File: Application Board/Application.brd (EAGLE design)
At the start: 101.6 x 101.6 mm, 54 parts, among them Q1 DMP2012SN-7, T1 FDN340P, T2 AP1117_LIN_REG, U1 LM3409HV'LM3409HV', X1 22-23-2101

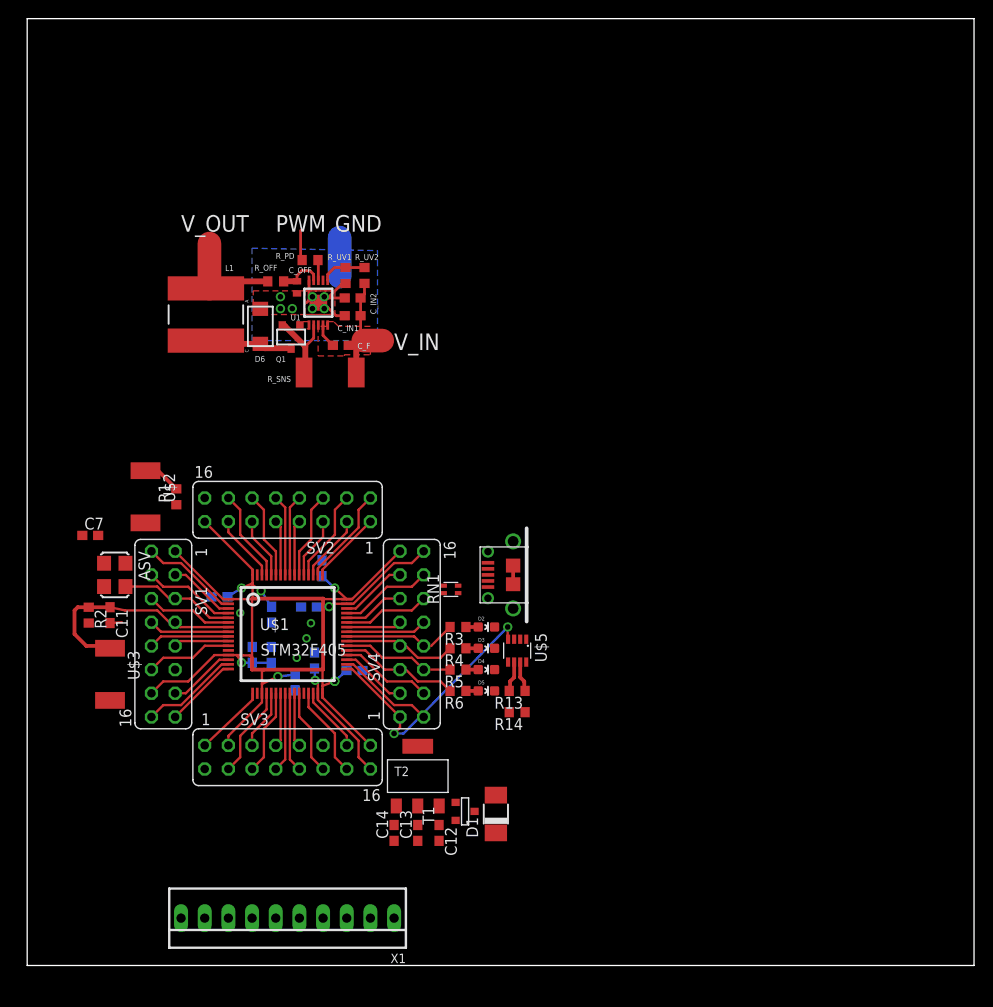
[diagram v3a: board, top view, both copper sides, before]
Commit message: Rearranged components, including LED driver.
Not finished, still need to fix LED driver and route the remaining
connector lines.
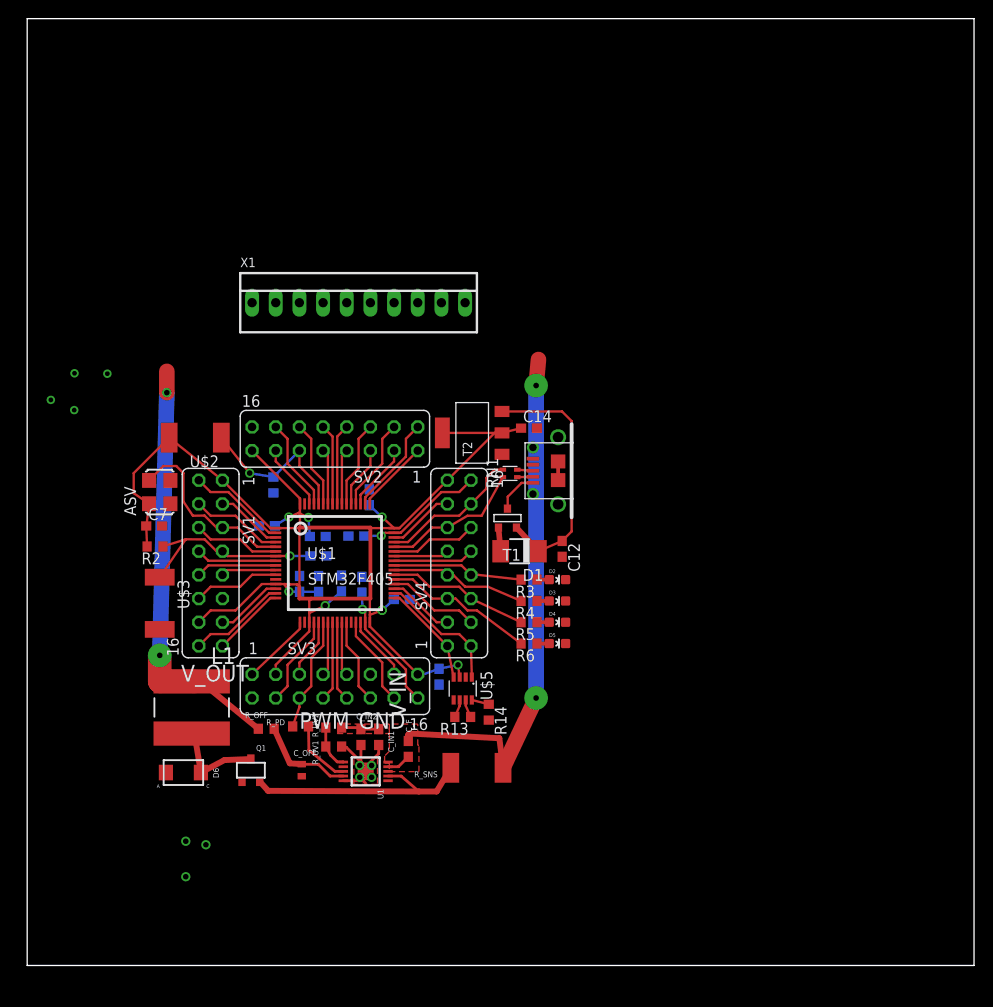
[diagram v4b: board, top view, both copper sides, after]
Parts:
- moved X1 66.5 mm to (35.6, 71.1), turned to 0 degrees
- moved C_OFF 51.8 mm to (29.5, 21.0)
- moved R_UV1 50.6 mm to (32.9, 23.5), turned to 180 degrees
- moved U1 50.5 mm to (36.3, 20.8), turned to 270 degrees
- moved R_PD 50.0 mm to (29.3, 25.7)
- moved R_UV2 48.6 mm to (32.9, 25.5), turned to 0 degrees
- moved D6 48.6 mm to (16.8, 20.7), turned to 180 degrees
- moved R_OFF 48.0 mm to (25.7, 25.4)
- moved C_IN2 47.1 mm to (35.8, 24.5), turned to 270 degrees
- moved Q1 46.7 mm to (24.0, 21.0), turned to 0 degrees
- moved C14 45.8 mm to (53.8, 57.7), turned to 0 degrees
- moved C_IN1 45.3 mm to (37.7, 24.5), turned to 270 degrees
- moved R_SNS 45.2 mm to (48.3, 21.2)
- moved C_F 43.9 mm to (40.9, 23.2), turned to 270 degrees
- moved L1 42.2 mm to (17.7, 27.7)
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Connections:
- removed net CAM_LED: SV3.6, U$1.22, X1.1
- removed net PWM: R_PD.1
- removed net V_IN: C_F.1, C_IN1.1, C_IN2.1, R_SNS.2, R_UV2.2, U1.10, U1.8
- removed net V_OUT: L1.2, R_OFF.1
- new net CAM_LEDV: L1.2, R_OFF.1, X1.1
- new net CAM_LED_PWM: R_PD.1, SV3.6, U$1.22
- net 12V: now also C_F.1, C_IN1.1, C_IN2.1, R_SNS.2, R_UV2.2, U1.10, U1.8
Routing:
- net 12V: track 0.00 -> 62.6 mm, vias 0 -> 2
- net CAM_LEDV: track 0.00 -> 51.5 mm, vias 0 -> 2
- net +3V3: track 115.3 -> 159.5 mm, vias 7 -> 8
- net N$58: track 0.00 -> 27.4 mm
- net N$8: track 8.91 -> 26.3 mm
- net CAN2_RX: track 28.2 -> 11.3 mm, vias 2 -> 0
- net V_OUT: track 16.8 -> 0.00 mm
- net CAM_LED_PWM: track 0.00 -> 12.4 mm
- net V_IN: track 12.3 -> 0.00 mm
- net CAM_LED: track 9.19 -> 0.00 mm
- net USBD-: track 6.57 -> 15.3 mm
- net OSCIN: track 12.4 -> 19.8 mm
- net BOOT0: track 11.0 -> 18.0 mm, vias 0 -> 1
- net GND: track 19.1 -> 13.3 mm
- net USBD+: track 9.95 -> 15.6 mm
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- added copper zone on layer 1, net 12V
- added copper zone on layer 1, net N$19
- removed copper zone on layer 16, net GND
- removed copper zone on layer 1, net N$10
- removed copper zone on layer 1, net V_IN

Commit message: updated stm... microcontroller to the updated version
organized order of output lines. Still not complete.
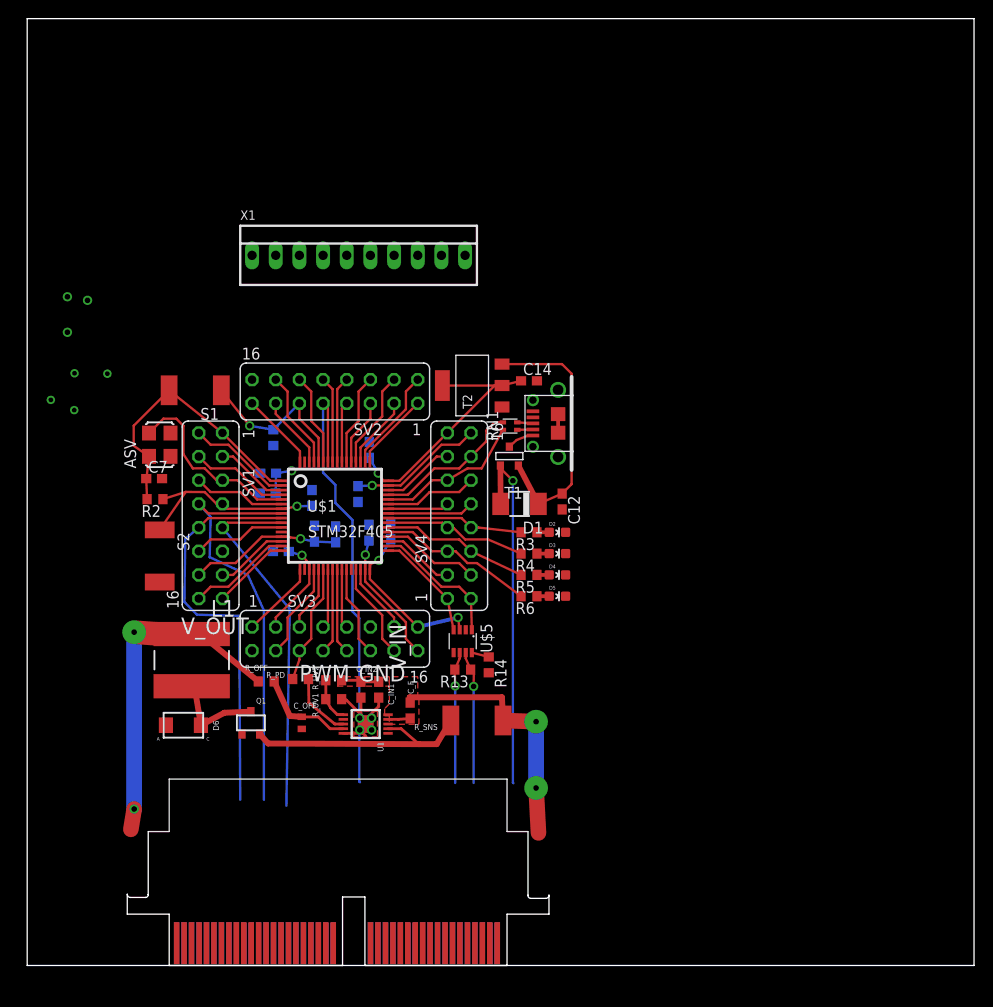
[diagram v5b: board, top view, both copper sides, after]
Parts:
- removed C13: 0.1uF, rcl:C0603
- removed U$2, U$3: SWITCH, DiscreteComponents:SW_2512
- added S1, S2: SWITCH, DiscreteComponents:SW_2512
- added U$6: HSCPART, Connectors:HSC8-40PINOUUT
- moved C4 7.40 mm to (39.0, 46.6), turned to 90 degrees
- moved C3 7.35 mm to (27.2, 44.4), turned to 0 degrees
- moved C8 7.11 mm to (25.8, 50.7), turned to 0 degrees
- moved T1 6.66 mm to (51.8, 54.7)
- moved C11 6.26 mm to (30.6, 50.2), turned to 90 degrees
- moved C6 5.64 mm to (25.9, 52.8)
- moved C1 5.64 mm to (36.7, 46.4)
- moved C10 5.62 mm to (30.8, 46.3)
- moved C9 5.61 mm to (33.1, 46.3)
- moved ASV 5.08 mm to (14.2, 55.9)
- moved C5 5.08 mm to (36.7, 55.3)
- moved D5 5.08 mm to (56.9, 39.6)
- moved R1 5.08 mm to (26.4, 56.6)
- moved R6 5.08 mm to (53.8, 39.6)
- moved RN1 5.08 mm to (51.8, 57.9)
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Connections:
- net +3V3: now also S1.2; no longer C13.1, U$2.2
- net BOOT0: now also S1.1; no longer U$2.1
- net GND: now also S2.2; no longer C13.2, U$3.2
- net NRST: now also S2.1; no longer U$3.1
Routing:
- net TEMP_SENS: track 5.93 -> 48.8 mm
- net +3V3: track 159.5 -> 118.0 mm, vias 8 -> 6
- net +5V: track 2.55 -> 38.7 mm, vias 0 -> 1
- net SHFT_REG_DATA: track 8.68 -> 44.5 mm
- net SHFT_REG_CLK: track 8.68 -> 44.1 mm
- net SHFT_REG_EN: track 5.93 -> 39.0 mm
- net 12V: track 62.6 -> 32.8 mm
- net CANH: track 1.93 -> 14.3 mm, vias 0 -> 1
- net CANL: track 1.93 -> 14.1 mm, vias 0 -> 1
- net CAM_LEDV: track 51.5 -> 42.2 mm
- net N$57: track 4.61 -> 2.89 mm
- net N$58: track 27.4 -> 28.6 mm
- net BOOT0: track 18.0 -> 18.6 mm
- net PIN59: track 9.32 -> 9.92 mm
- net PIN54: track 9.32 -> 9.92 mm
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
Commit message: Fixed output voltages and signal paths, added connector
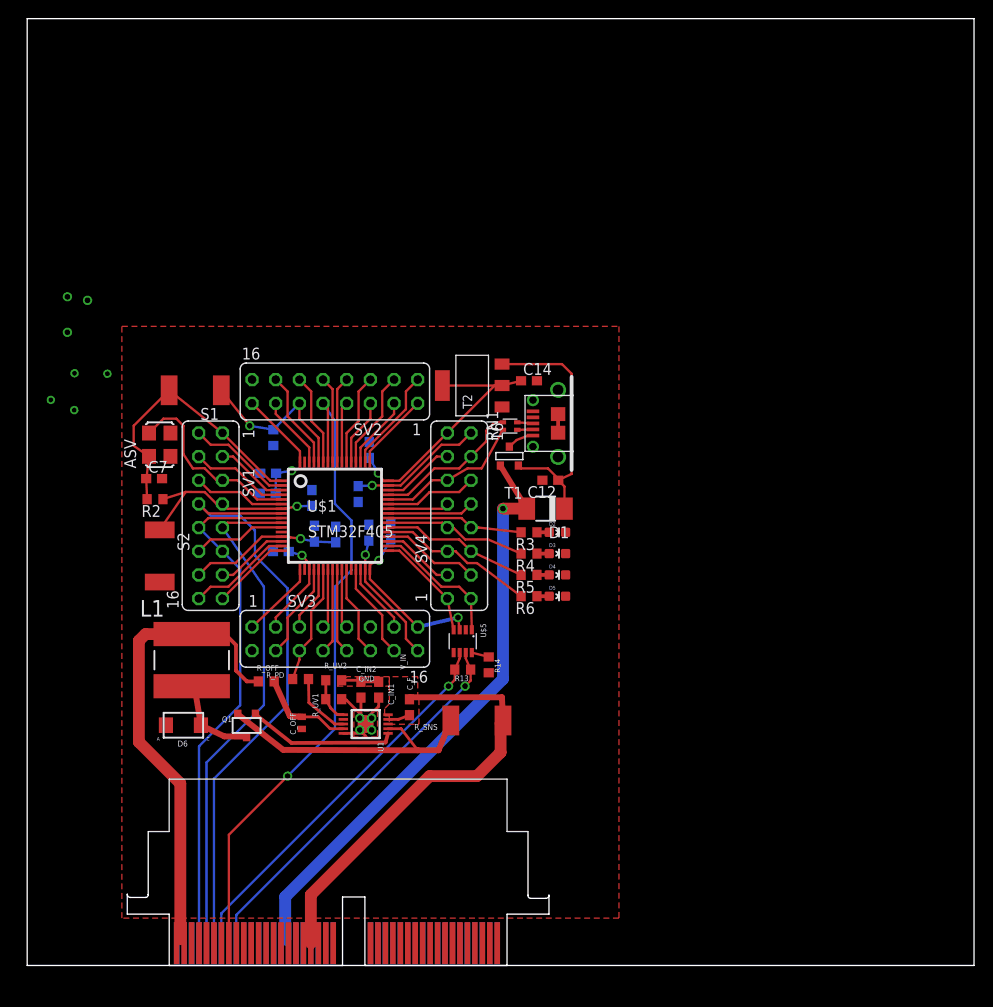
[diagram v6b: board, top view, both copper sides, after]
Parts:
- removed X1: 22-23-2101, con-molex:22-23-2101
- moved D1 2.84 mm to (55.6, 49.0)
- moved C12 2.62 mm to (56.1, 52.1), turned to 180 degrees
- moved Q1 0.54 mm to (23.5, 25.8), turned to 180 degrees
- moved C_F 0.36 mm to (41.0, 27.7)
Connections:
- net +5V: now also U$6.B15, U$6.B16; no longer X1.9
- net 12V: now also U$6.T18, U$6.T19, U$6.T20; no longer X1.10
- net CAM_LEDV: now also U$6.T1, U$6.T2; no longer X1.1
- net CANH: now also U$6.B9; no longer X1.7
- net CANL: now also U$6.B7; no longer X1.6
- net GND: now also U$6.T11, U$6.T12, U$6.T13; no longer X1.8
- net SHFT_REG_CLK: now also U$6.B4; no longer X1.3
- net SHFT_REG_DATA: now also U$6.B6; no longer X1.4
- net SHFT_REG_EN: now also U$6.B5; no longer X1.2
- net TEMP_SENS: now also U$6.T8; no longer X1.5
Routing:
- net CANL: track 14.1 -> 41.7 mm
- net CANH: track 14.3 -> 41.7 mm
- net +5V: track 38.7 -> 65.8 mm
- net TEMP_SENS: track 48.8 -> 71.0 mm, vias 0 -> 1
- net 12V: track 32.8 -> 54.0 mm, vias 2 -> 0
- net SHFT_REG_DATA: track 44.5 -> 65.5 mm
- net SHFT_REG_EN: track 39.0 -> 55.1 mm
- net N$10: track 0.00 -> 16.1 mm
- net SHFT_REG_CLK: track 44.1 -> 57.5 mm
- net CAM_LEDV: track 42.2 -> 52.1 mm, vias 2 -> 0
- net N$8: track 26.3 -> 30.7 mm
- net L1: track 10.1 -> 9.56 mm
- added copper zone on layer 1, net N$20
- removed copper zone on layer 1, net N$19
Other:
- board text removed: "PWM"
- board text removed: "V_OUT"

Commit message: Fixed up some wiring
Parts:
- renumbered U$6 to U$2
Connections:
- removed net 12V: C_F.1, C_IN1.1, C_IN2.1, R_SNS.2, R_UV2.2, U$2.T18, U$2.T19, U$2.T20, U1.10, U1.8
- new net +12V: C_F.1, C_IN1.1, C_IN2.1, R_SNS.2, R_UV2.2, U$2.T10, U$2.T11, U$2.T12, U$2.T13, U$2.T7, U$2.T8, U$2.T9, U1.10, U1.8
- net +3V3: now also U$2.B24
- net +5V: now also U$2.B1, U$2.B2, U$2.B3, U$2.B4, U$2.B5, U$2.B6; no longer U$2.B15, U$2.B16
- net CAM_LEDV: no longer U$2.T1, U$2.T2
- net CANH: now also U$2.B35; no longer U$2.B9
- net CANL: now also U$2.B33; no longer U$2.B7
- net GND: now also U$2.T14, U$2.T15, U$2.T16, U$2.T17, U$2.T18, U$2.T19, U$2.T20; no longer U$2.T11, U$2.T12, U$2.T13
- net SHFT_REG_CLK: no longer U$2.B4
- net SHFT_REG_DATA: no longer U$2.B6
- net SHFT_REG_EN: no longer U$2.B5
- net TEMP_SENS: now also U$2.B25; no longer U$2.T8
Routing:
- net TEMP_SENS: track 71.0 -> 6.53 mm, vias 1 -> 0
- net 12V: track 54.0 -> 0.00 mm
- net CANH: track 41.7 -> 1.93 mm, vias 1 -> 0
- net CANL: track 41.7 -> 1.93 mm, vias 1 -> 0
- net +5V: track 65.8 -> 27.5 mm
- net +12V: track 0.00 -> 31.2 mm
- net SHFT_REG_CLK: track 57.5 -> 36.4 mm
- net SHFT_REG_EN: track 55.1 -> 35.7 mm
- net SHFT_REG_DATA: track 65.5 -> 47.8 mm
- net CAM_LEDV: track 52.1 -> 51.3 mm
- net GND: vias 11 -> 15
- added copper zone on layer 16, net GND
- removed copper zone on layer 1, net N$20

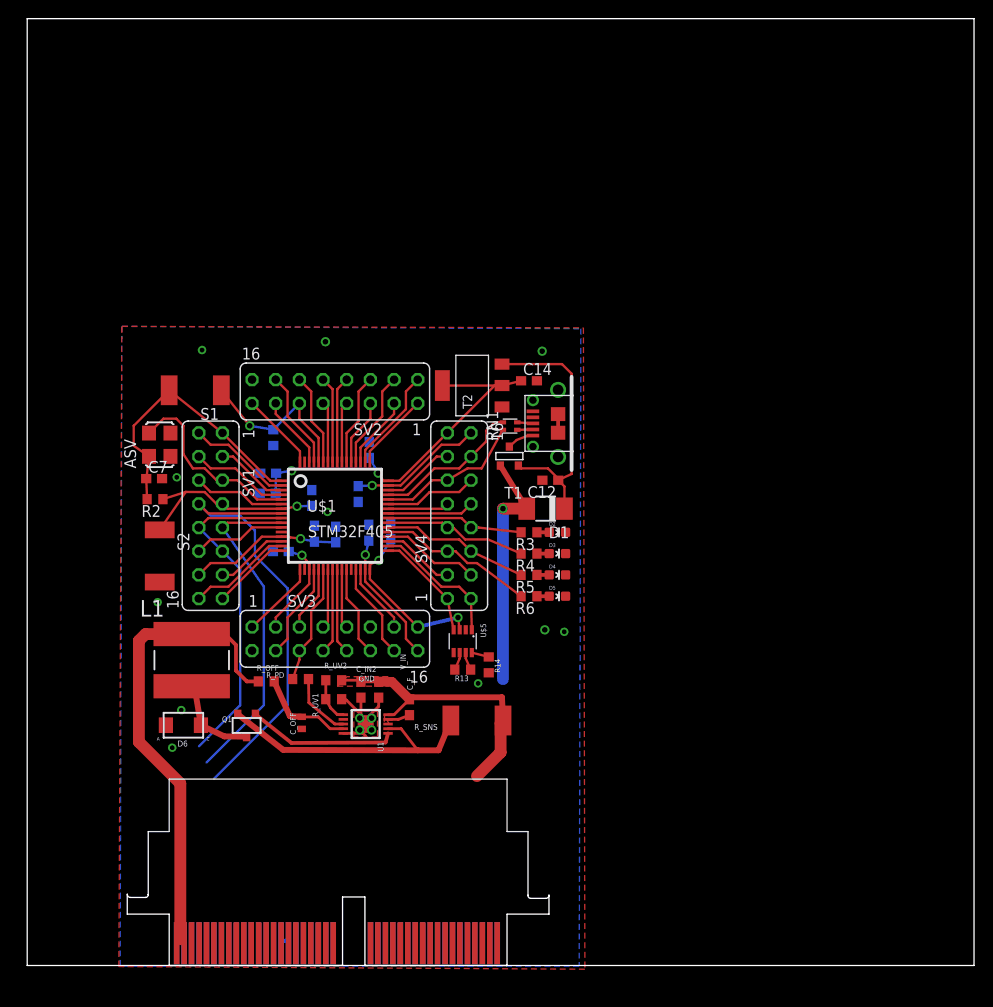
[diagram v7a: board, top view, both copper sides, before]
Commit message: fixed some connections
Have been trying to solve some problems with some polygons and haven't
been able to fix other issues.
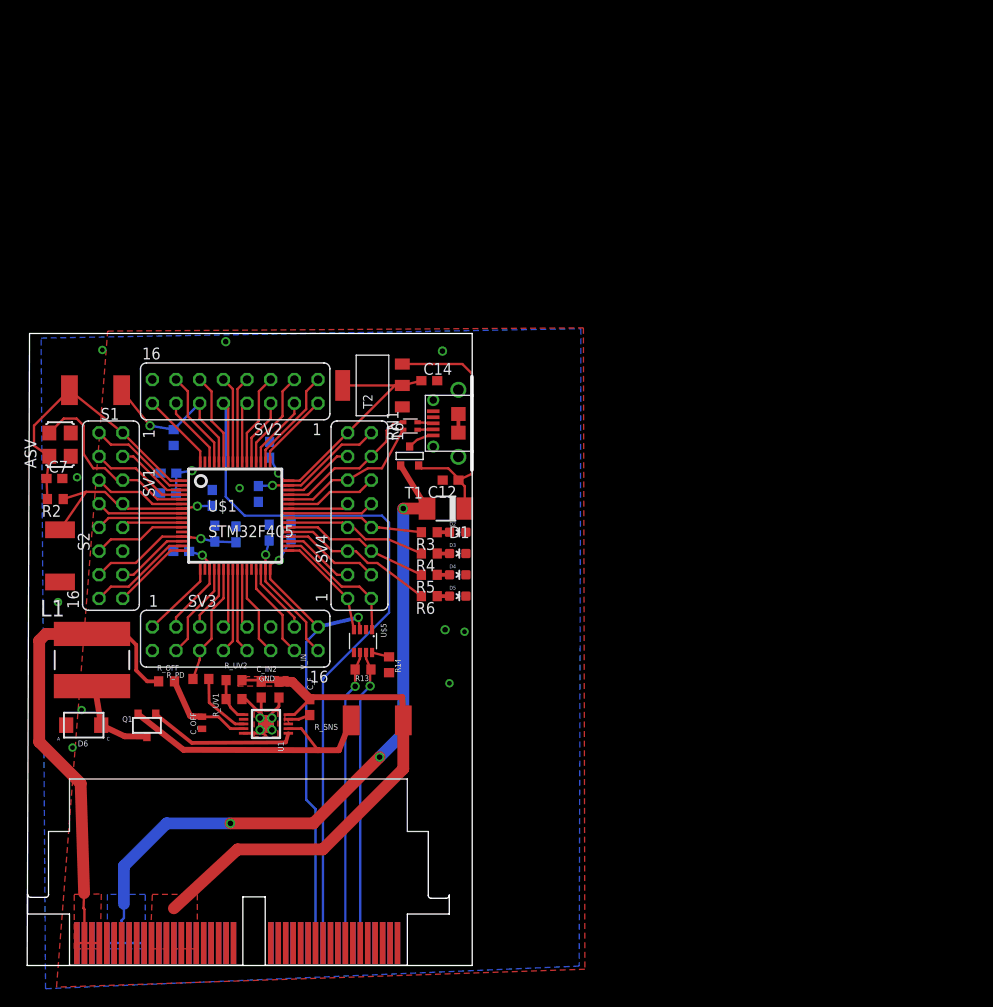
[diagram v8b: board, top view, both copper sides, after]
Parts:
- moved C2 10.7 mm to (24.8, 50.6)
- moved C4 10.7 mm to (28.3, 46.6)
- moved SV2 10.7 mm to (22.3, 61.6)
- moved SV3 10.7 mm to (22.3, 35.1)
- moved U$1 10.7 mm to (22.3, 48.3)
- moved U1 10.7 mm to (25.6, 25.9)
- moved ASV 10.7 mm to (3.53, 55.9)
- moved C10 10.7 mm to (20.1, 46.3)
- moved C11 10.7 mm to (19.9, 50.2)
- moved C12 10.7 mm to (45.4, 52.1)
- moved C14 10.7 mm to (43.1, 62.7)
- moved C3 10.7 mm to (16.5, 44.4)
- moved C5 10.7 mm to (26.0, 55.3)
- moved C6 10.7 mm to (15.2, 52.8)
- moved C7 10.7 mm to (2.93, 52.3)
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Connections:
- net SHFT_REG_CLK renamed PIN9
- net SHFT_REG_DATA renamed PIN8
- net SHFT_REG_EN renamed PIN10
- net +12V: now also U$2.T14, U$2.T15, U$2.T16, U$2.T17; no longer U$2.T10, U$2.T7, U$2.T8, U$2.T9
- net +3V3: now also U$2.B29; no longer U$2.B24
- net +5V: now also U$2.B10, U$2.B7, U$2.B8, U$2.B9; no longer U$2.B1, U$2.B2, U$2.B3, U$2.B4
- net CAM_LEDV: now also U$2.T1, U$2.T2, U$2.T3, U$2.T4
- net GND: now also U$2.T21, U$2.T22, U$2.T23, U$2.T24, U$2.T25, U$2.T26; no longer U$2.T14, U$2.T15, U$2.T16, U$2.T17, U$2.T18
- net TEMP_SENS: now also U$2.B30; no longer U$2.B25
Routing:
- net TEMP_SENS: track 6.53 -> 83.4 mm
- net +5V: track 27.5 -> 80.6 mm, vias 1 -> 3
- net PIN8: track 47.8 -> 9.28 mm
- net +3V3: track 118.0 -> 152.8 mm
- net CANH: track 1.93 -> 31.8 mm, vias 0 -> 1
- net CANL: track 1.93 -> 31.7 mm, vias 0 -> 1
- net PIN10: track 35.7 -> 6.53 mm
- net +12V: track 31.2 -> 59.9 mm
- net PIN9: track 36.4 -> 9.28 mm
- net CAM_LEDV: track 51.3 -> 53.6 mm
- added copper zone on layer 1, net +12V
- added copper zone on layer 16, net +5V
- added copper zone on layer 1, net CAM_LEDV
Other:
- board size 101.6 x 101.6 mm -> 47.8 x 67.8 mm
